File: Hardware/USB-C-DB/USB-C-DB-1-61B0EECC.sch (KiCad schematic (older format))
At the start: 152 parts, among them J23 +5V, J24 PWM_BC, J25 GND, Q10 XP262N7002TR-G, Q3 XP262N7002TR-G, Q4 XP262N7002TR-G, Q5 XP262N7002TR-G, Q6 XP262N7002TR-G, Q7 XP262N7002TR-G, Q8 XP262N7002TR-G, Q9 XP262N7002TR-G, U10 NA555D, U5 74HC595_mod, U6 74HC595, U7 74HC595, U8 74HC595, U9 74HC595

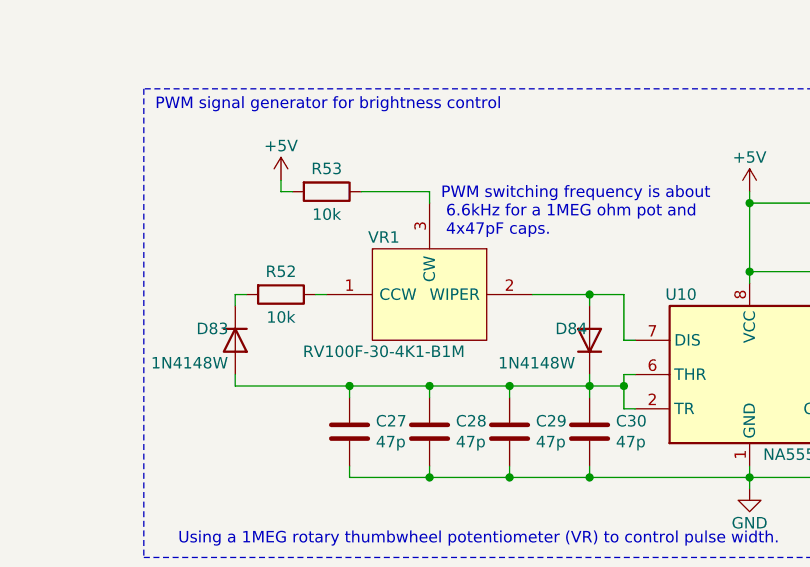
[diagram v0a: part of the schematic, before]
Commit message: Adding OSHW logo on PCB
* Updating BOM with available parts for test run
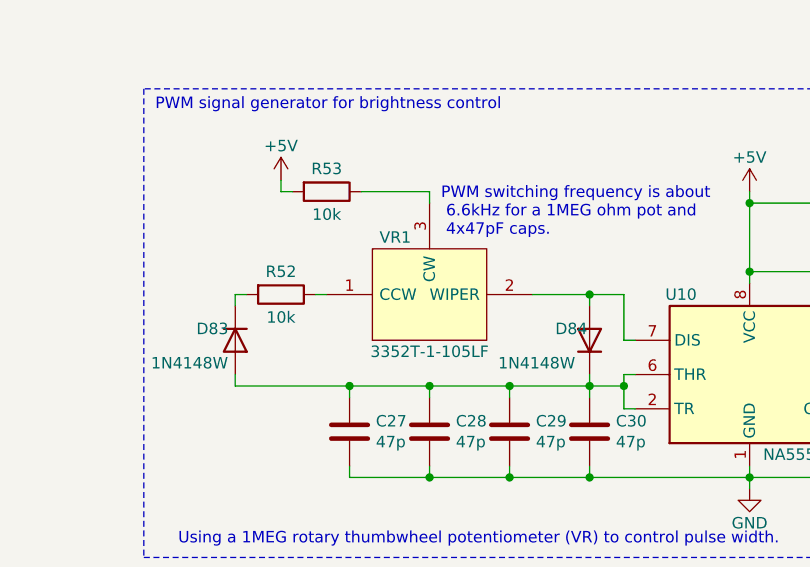
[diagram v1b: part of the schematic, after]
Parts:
- removed VR1: RV100F-30-4K1-B1M, Mouser-imports:RV100F304K1B1M, symbol USB-C-DB-rescue:RV100F-30-4K1-B1M
- added VR1: 3352T-1-105LF, Mouser-imports:3352T1103LF, symbol USB-C-DB-rescue:3352T-1-105LF
- C17, C19, C21, C23, C25: MPN prod (none) -> CL21B105KBFNNNG
- C18, C20, C22, C24, C26, C32: MPN prod (none) -> C0805C104M5RACTU
- C27, C28, C29, C30, C31: MPN prod (none) -> C0402C470J5GACTU
- D1, D10, D11, D12, D13, D14, D15, D16, D17, D18, D19, D2, D20, D21, D22, D23, D24, D25, D26, D27, D28, D29, D3, D30, D31, D32, D33, D34, D35, D36, D37, D38, D39, D4, D40, D41, D42, D43, D44, D45, D46, D47, D48, D49, D5, D50, D51, D52, D53, D54, D55, D56, D57, D58, D59, D6, D60, D61, D62, D63, D64, D65, D66, D67, D68, D69, D7, D70, D71, D72, D73, D74, D75, D76, D77, D78, D79, D8, D80, D9: MPN prod (none) -> CLV1L-FKB-CJ1N1E1BB7B3B3
- D81, D82: MPN prod (none) -> CLA1A-WKB-CWbYa153
- D83, D84: MPN prod (none) -> 1N4148W_R1_00001
- Q10, Q3, Q4, Q5, Q6, Q7, Q8, Q9: MPN prod (none) -> XP262N7002TR-G
- R20, R21, R23, R24, R26, R27, R29, R30, R32, R33, R35, R36, R38, R39, R41, R42, R44, R45, R47, R48: MPN prod (none) -> RT0603DRE07583RL
- R22, R25, R28, R31, R34, R37, R40, R43, R46, R49, R50, R51: MPN prod (none) -> RC0603FR-07309RL
- R52, R53: MPN prod (none) -> CRG0603F10K/10
- U10: MPN prod (none) -> NA555DR
- U5, U6, U7, U8, U9: MPN prod (none) -> MC74HC595ADTG
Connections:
- net at R52.1: now also VR1.1 (CCW)
- net at D84.2 (A), U10.7 (DIS): now also VR1.2 (WIPER)
- net at R53.1: now also VR1.3 (CW)

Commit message: Updating schematic to replace FT260 for FT231
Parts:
- removed J23: +5V, TestPoint:TestPoint_Pad_D1.0mm, symbol Connector_Generic:Conn_01x01
- removed J25: GND, TestPoint:TestPoint_Pad_D1.0mm, symbol Connector_Generic:Conn_01x01
- renumbered C17 to C14, C18 to C15, C19 to C16, C20 to C17, C21 to C18, C22 to C19, C23 to C20, C24 to C21, C25 to C22, C26 to C23, C27 to C24, C28 to C25, C29 to C26, C30 to C27, C31 to C28, C32 to C29, D7 to D10, D8 to D11, D9 to D12, D10 to D13, D11 to D14, D12 to D15, D13 to D16, D14 to D17, D15 to D18, D16 to D19, D17 to D20, D18 to D21, D19 to D22, D20 to D23, D21 to D24, D22 to D25, D23 to D26, D24 to D27, D25 to D28, D26 to D29, D27 to D30, D28 to D31, D29 to D32, D30 to D33, D31 to D34, D32 to D35, D33 to D36, D34 to D37, D35 to D38, D36 to D39, D1 to D4, D37 to D40, D38 to D41, D39 to D42, D40 to D43, D41 to D44, D42 to D45, D43 to D46, D44 to D47, D45 to D48, D46 to D49, D2 to D5, D47 to D50, D48 to D51, D49 to D52, D50 to D53, D51 to D54, D52 to D55, D53 to D56, D54 to D57, D55 to D58, D56 to D59, D3 to D6, D57 to D60, D58 to D61, D59 to D62, D60 to D63, D61 to D64, D62 to D65, D63 to D66, D64 to D67, D65 to D68, D66 to D69, D4 to D7, D67 to D70, D68 to D71, D69 to D72, D70 to D73, D71 to D74, D72 to D75, D73 to D76, D74 to D77, D75 to D78, D76 to D79, D5 to D8, D77 to D80, D78 to D81, D79 to D82, D80 to D83, D81 to D84, D82 to D85, D83 to D86, D84 to D87, D6 to D9, J24 to J16, R20 to R13, R21 to R14, R22 to R15, R23 to R16, R24 to R17, R25 to R18, R26 to R19, R27 to R20, R28 to R21, R29 to R22, R30 to R23, R31 to R24, R32 to R25, R33 to R26, R34 to R27, R35 to R28, R36 to R29, R37 to R30, R38 to R31, R39 to R32, R40 to R33, R41 to R34, R42 to R35, R43 to R36, R44 to R37, R45 to R38, R46 to R39, R47 to R40, R48 to R41, R49 to R42, R50 to R43, R51 to R44, R52 to R45, R53 to R46
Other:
- note added: "Test points"
- note removed: "Test points (bottom side)"
- moved on the sheet: J16

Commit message: Fixing incorrect connection in debug LEDs
* Updating symbol to fix incorrect GND connection in debug LED
* Adding image of assembled demo
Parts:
- D84, D85: symbol Device:LED -> USB-C-DB-rescue:LED
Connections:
- net GND: now also D84.4 (K), D85.4 (K); no longer D84.1 (K), D85.1 (K)
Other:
- note added: "01-11-2022"
- note added: "v0.5.1"
- note removed: "11-03-2022"
- note removed: "v0.5"
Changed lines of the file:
@@
 USB-C demo board for Micro-controllers
 Text Notes 12950 11050 0    50   ~ 0
-11-03-2022
+01-11-2022
 Text Notes 15450 11050 0    50   ~ 0
-v0.5
+v0.5.1
 Wire Wire Line
 	10750 2650 10750 2900
@@
 	10300 2500 10300 2600
 $Comp
-L Device:LED D?
+L USB-C-DB-rescue:LED D?
 U 1 1 74F7CED4
 P 10750 3400
@@
 Mini display board for testing and evaluating a USB Type-C interface for Micro-controllers.
 $Comp
-L Device:LED D?
+L USB-C-DB-rescue:LED D?
 U 1 1 61B1368E
 P 11050 3400

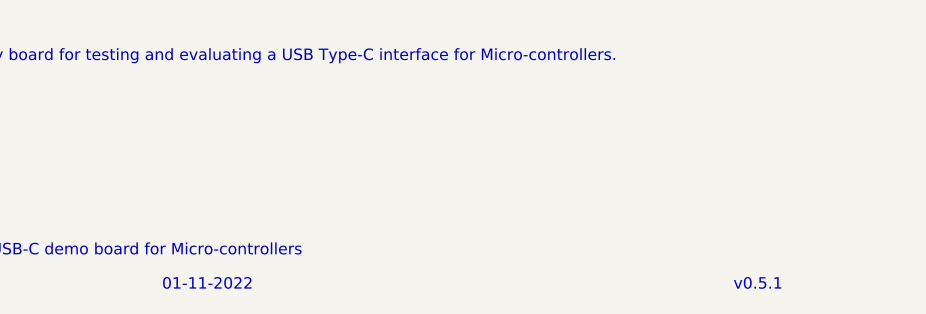
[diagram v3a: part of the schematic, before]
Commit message: Updating OSHW logo to include mechanicals
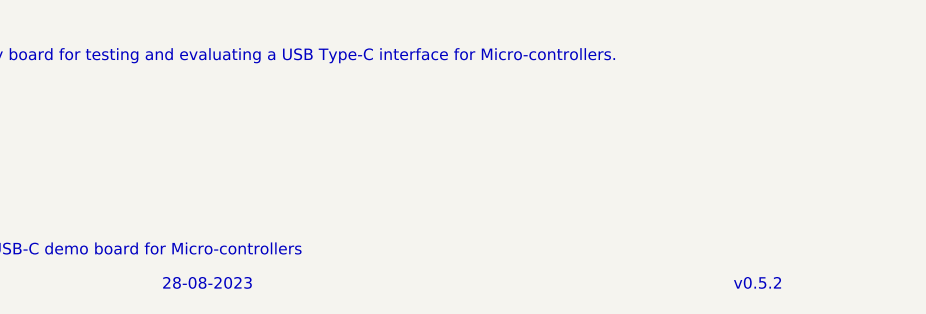
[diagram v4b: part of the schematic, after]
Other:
- note added: "28-08-2023"
- note added: "v0.5.2"
- note removed: "01-11-2022"
- note removed: "v0.5.1"
